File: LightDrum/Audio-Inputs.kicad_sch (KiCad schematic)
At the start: 52 parts, among them J201 XLR3, J202 SJ-43515RS-SMT-TR, Q201 NX6008NBKWX, Q202 NX6008NBKWX, U201 MCP3561R, U202 AZV321, U203 MCP3561R, U204 AZV321, U205 AZV321, U206 OPA1652

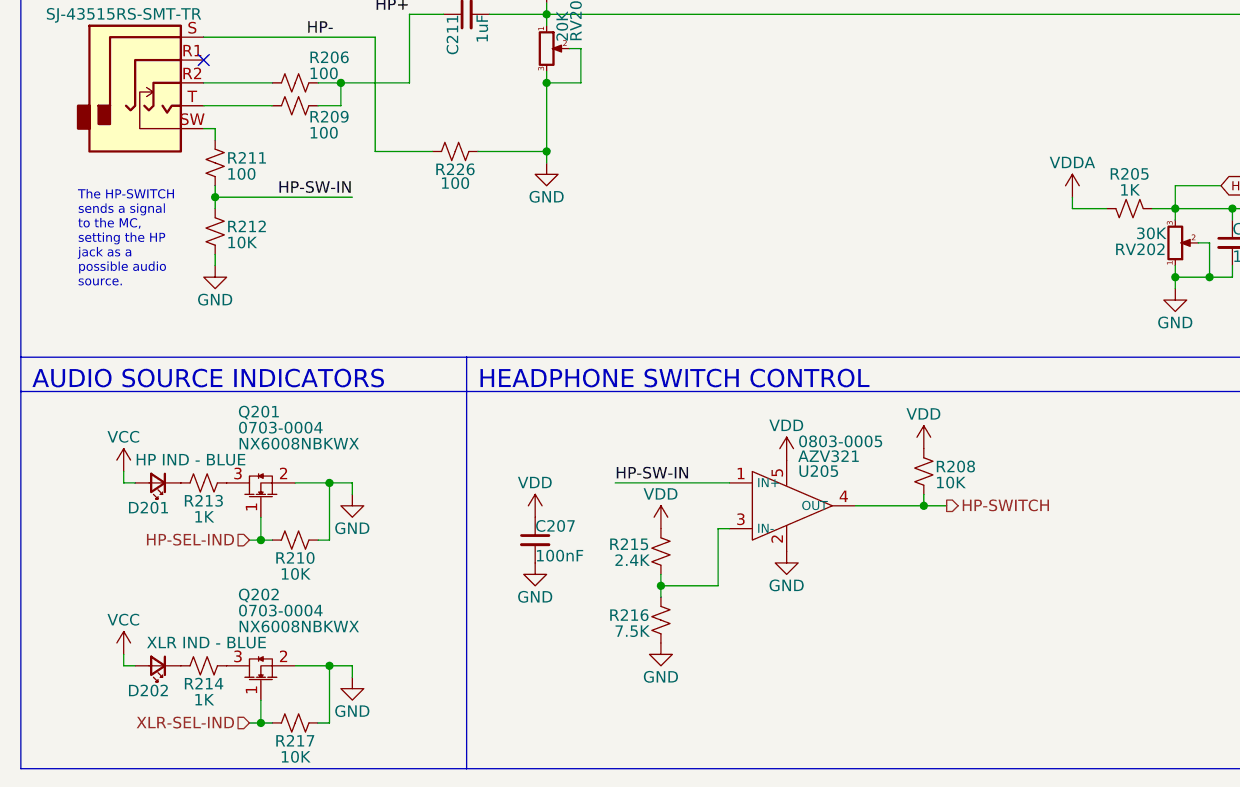
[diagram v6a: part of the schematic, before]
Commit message: Start REV 10 - Fix small issues
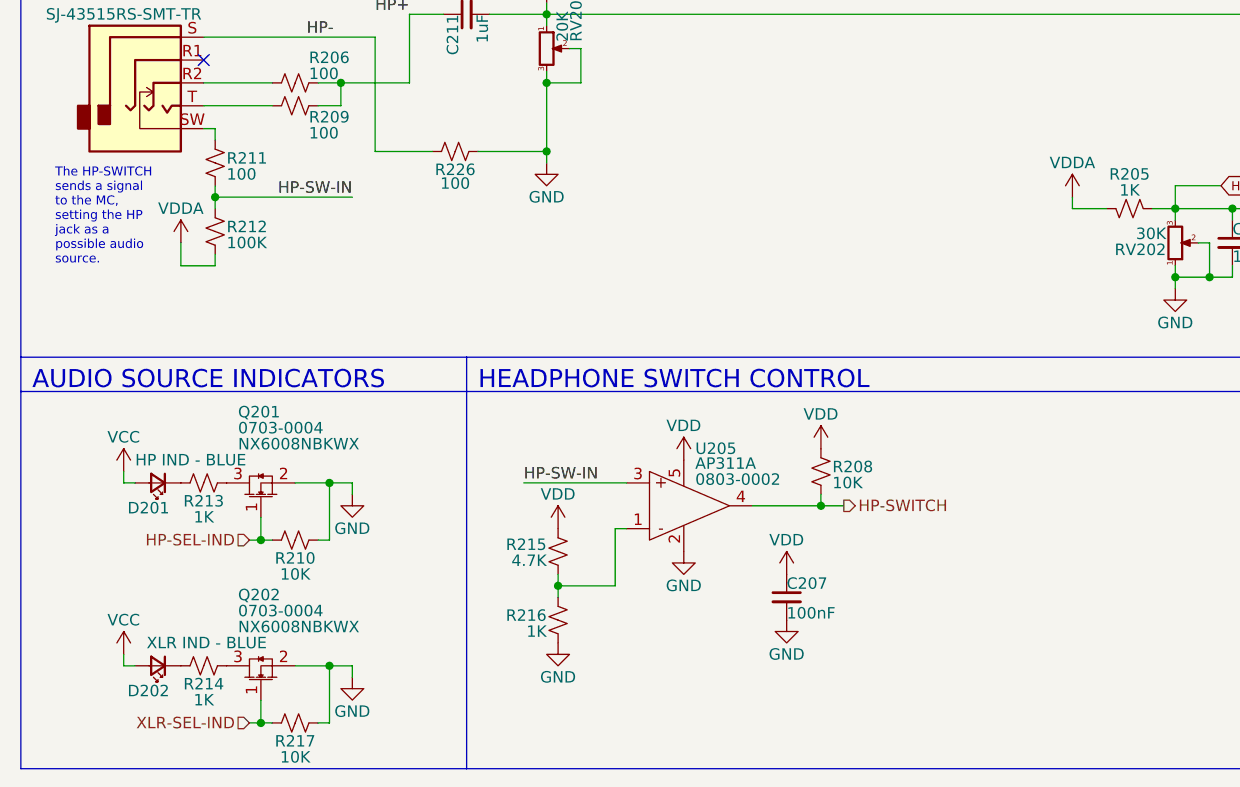
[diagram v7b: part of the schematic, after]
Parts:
- removed U205: AZV321, Package_TO_SOT_SMD:SOT-23-5, symbol Daxxn_OPAMP:AZV321
- added U205: AP311A, Package_TO_SOT_SMD:SOT-23-5, symbol Daxxn_OPAMP:AP311A
- R212: value 10K -> 100K
- R215: value 2.4K -> 4.7K
- R216: value 7.5K -> 1K
- RV203, RV204: footprint Potentiometer_SMD:Potentiometer_Bourns_3214W_Vertical -> Daxxn_Switches:Bourns_3214W_Vertical
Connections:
- net AGND: now also U205.2; no longer R212.1
- net HP-SW-IN: now also U205.3
- net HP-SWITCH: now also U205.4
- net VDD: now also U205.5
- net VDDA: now also R212.1
- net at R215.1, R216.2: now also U205.1
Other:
- moved on the sheet: C207, R208, R215, R216
